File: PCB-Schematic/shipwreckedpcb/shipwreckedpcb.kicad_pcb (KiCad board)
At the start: 4 copper layers, 61.8 x 79.6 mm, 153 parts, among them J1 USB4105, J2 Waveshare 1.54" E-Ink, J3 GPIO, J4 GPIO, J5 SWD, Q1 Si1308EDL, SW1 BOOTSEL, SW10 Resistive, SW11 Clicky - THT, SW12 Clicky - SMD, SW13 Clicky - THT, SW14 Clicky - SMD, SW15 Clicky - THT, SW16 Clicky - SMD, SW17 Clicky - THT, SW18 Clicky - SMD, SW19 PWR Switch, SW2 RESET, SW3 Resistive, SW4 Resistive, SW5 Resistive, SW6 Resistive, SW7 Resistive, SW8 Resistive, SW9 Resistive, U1 RP2040, U2 W25Q128JVS, U3 Si4463, U4 TPS61200DRC, U5 AS179-92LF, U7 PCA9555PW, U8 ST25DV04K-IE6S3, Y1 ABM8-272-T3, Y2 X322530MOB4SI

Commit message: finish placing components
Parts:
- added J14: Conn_01x01, Connector_Wire:SolderWirePad_1x01_SMD_1x2mm, B.Cu at (117.6, 93.7)
- added J15: Conn_01x01, Connector_Wire:SolderWirePad_1x01_SMD_1x2mm, B.Cu at (117.6, 95.5)
- added J16: Conn_01x01, Connector_Wire:SolderWirePad_1x01_SMD_1x2mm, B.Cu at (117.6, 97.3)
- added J17: Conn_01x01, Connector_Wire:SolderWirePad_1x01_SMD_1x2mm, B.Cu at (117.6, 99.1)
- added J18: Conn_01x01, Connector_Wire:SolderWirePad_1x01_SMD_1x2mm, B.Cu at (117.6, 100.9)
- added J19: Conn_01x01, Connector_Wire:SolderWirePad_1x01_SMD_1x2mm, B.Cu at (117.6, 102.7)
- added J20: Conn_01x01, Connector_Wire:SolderWirePad_1x01_SMD_1x2mm, B.Cu at (117.6, 104.5)
- added J21: Conn_01x01, Connector_Wire:SolderWirePad_1x01_SMD_1x2mm, B.Cu at (117.6, 106.3)
- added J22: Conn_01x01, Connector_Wire:SolderWirePad_1x01_SMD_1x2mm, B.Cu at (117.6, 108.1)
- added J23: Conn_01x01, Connector_Wire:SolderWirePad_1x01_SMD_1x2mm, B.Cu at (117.6, 109.9)
- added J24: Conn_01x01, Connector_Wire:SolderWirePad_1x01_SMD_1x2mm, B.Cu at (117.6, 111.7)
- added J25: Conn_01x01, Connector_Wire:SolderWirePad_1x01_SMD_1x2mm, B.Cu at (117.6, 113.6)
- added J26: Conn_01x01, Connector_Wire:SolderWirePad_1x01_SMD_1x2mm, B.Cu at (117.6, 115.4)
- added J28: Conn_01x01, Connector_Wire:SolderWirePad_1x01_SMD_1x2mm, B.Cu at (117.6, 117.2)
- added J29: Conn_01x01, Connector_Wire:SolderWirePad_1x01_SMD_1x2mm, B.Cu at (176.3, 127.8)
- added J30: Conn_01x01, Connector_Wire:SolderWirePad_1x01_SMD_1x2mm, B.Cu at (176.3, 125.4)
- added J31: Conn_01x01, Connector_Wire:SolderWirePad_1x01_SMD_1x2mm, B.Cu at (176.4, 102.0)
- added J32: Conn_01x01, Connector_Wire:SolderWirePad_1x01_SMD_1x2mm, B.Cu at (176.4, 100.2)
- added J33: Conn_01x01, Connector_Wire:SolderWirePad_1x01_SMD_1x2mm, B.Cu at (176.4, 98.4)
- added J34: Conn_01x01, Connector_Wire:SolderWirePad_1x01_SMD_1x2mm, B.Cu at (176.4, 96.5)
- added J35: Conn_01x01, Connector_Wire:SolderWirePad_1x01_SMD_1x2mm, B.Cu at (176.4, 94.7)
- added J36: Conn_01x01, Connector_Wire:SolderWirePad_1x01_SMD_1x2mm, B.Cu at (176.4, 92.8)
- added J37: Conn_01x01, Connector_Wire:SolderWirePad_1x01_SMD_1x2mm, B.Cu at (176.4, 91.0)
- added J38: Conn_01x01, Connector_Wire:SolderWirePad_1x01_SMD_1x2mm, B.Cu at (176.4, 89.1)
- added J39: Conn_01x01, Connector_Wire:SolderWirePad_1x01_SMD_1x2mm, B.Cu at (176.4, 87.3)
- added J6: Conn_01x01, Connector_Wire:SolderWirePad_1x01_SMD_1x2mm, B.Cu at (117.6, 90.1)
- added J7: Conn_01x01, Connector_Wire:SolderWirePad_1x01_SMD_1x2mm, B.Cu at (117.6, 91.9)
- C25, C26, C27, C28, C29, C30, C31, C32, C33, C34, C35, C36, C37, C38, C39, C40, D21, D22, D23, D24, D25, D26, D27, D28, D29, D30, D31, D32, D33, D34, D35, D36, R10, R11, R12, R13, R14, R15, R16, R17: moved to B.Cu
- J3, J4: value GPIO -> Conn_01x01; footprint Connector_PinSocket_2.54mm:PinSocket_1x18_P2.54mm_Vertical -> Connector_Wire:SolderWirePad_1x01_SMD_1x2mm; moved to B.Cu
- moved C26 164.2 mm to (170.0, 120.2)
- moved C32 163.5 mm to (169.9, 86.3)
- moved C27 162.7 mm to (170.2, 109.3)
- moved J4 161.3 mm to (117.6, 88.3), turned to -90 degrees
- moved C28 157.6 mm to (165.6, 100.0), turned to 180 degrees
- moved J3 156.4 mm to (117.6, 86.5), turned to -90 degrees
- moved C31 154.3 mm to (160.4, 82.9), turned to 180 degrees
- moved C34 153.1 mm to (158.6, 130.5), turned to 180 degrees
- moved C30 144.6 mm to (151.0, 82.6), turned to -90 degrees
- moved C36 140.1 mm to (146.2, 131.5)
- moved D25 137.2 mm to (169.9, 89.2), turned to 180 degrees
- moved D21 131.9 mm to (170.0, 134.2), turned to 180 degrees
- moved C25 131.3 mm to (170.1, 131.4), turned to 0 degrees
- moved D24 131.2 mm to (169.2, 100.0), turned to -90 degrees
- moved D23 128.8 mm to (170.2, 112.1), turned to 180 degrees
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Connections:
- J4 pad 1: Earth -> +3V3
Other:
- outline, holes or cut-outs redrawn

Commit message: start routing
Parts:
- moved C29 4.95 mm to (132.3, 85.4), turned to -90 degrees
- moved C2 1.64 mm to (153.9, 108.8)
- moved R6 1.59 mm to (151.7, 111.2), turned to 90 degrees
- moved R1 0.74 mm to (152.9, 105.8)
- moved C7 0.57 mm to (152.4, 107.3)
- moved C15 0.53 mm to (150.8, 123.0)
- moved Q1 0.53 mm to (154.5, 123.0)
- moved R9 0.53 mm to (152.3, 123.0)
- moved C16 0.53 mm to (145.9, 123.0)
- moved C17 0.53 mm to (144.4, 123.0)
- moved C18 0.53 mm to (142.9, 123.0)
- moved C19 0.53 mm to (141.4, 123.0)
- moved C20 0.53 mm to (139.9, 123.0)
- moved C51 0.46 mm to (142.7, 72.5)
- moved C1 0.42 mm to (140.2, 105.5)
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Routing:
- net /SI_NSEL: track 0.00 -> 71.3 mm, vias 0 -> 2
- net /SI_NIRQ: track 0.00 -> 71.2 mm, vias 0 -> 2
- net /I2C_SDA: track 0.00 -> 46.8 mm, vias 0 -> 4
- net /I2C_SCL: track 0.00 -> 46.0 mm, vias 0 -> 4
- net /USB_DM: track 0.00 -> 42.3 mm, vias 0 -> 2
- net /USB_DP: track 0.00 -> 41.7 mm, vias 0 -> 2
- net /SPI_MISO: track 0.00 -> 31.4 mm
- net /SPI_MOSI: track 0.00 -> 28.3 mm, vias 0 -> 2
- net /SPI_CLK: track 0.00 -> 26.7 mm
- net /IO_INT: track 0.00 -> 26.6 mm
- net Net-(D4-A): track 0.00 -> 25.6 mm
- net /DISP_PREVGL: track 0.00 -> 20.3 mm, vias 0 -> 2
- net +3V3: track 0.00 -> 19.4 mm
- net /QSPI_SD3: track 0.00 -> 17.9 mm, vias 0 -> 2
- net /QSPI_SCLK: track 0.00 -> 15.6 mm, vias 0 -> 2
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
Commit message: production files (tentative)
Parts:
- moved SW19 16.9 mm to (133.9, 64.2), turned to 0 degrees
- moved C55 11.5 mm to (119.0, 68.3), turned to 90 degrees
- moved R18 11.4 mm to (121.5, 72.0), turned to 0 degrees
- moved R19 10.6 mm to (123.8, 72.7), turned to -90 degrees
- moved C54 9.53 mm to (120.5, 68.3), turned to 90 degrees
- moved C52 7.59 mm to (122.0, 68.3), turned to -90 degrees
- moved U4 5.15 mm to (124.9, 69.0), turned to -90 degrees
- moved C53 3.76 mm to (127.8, 68.3), turned to 90 degrees
- moved L9 1.68 mm to (126.1, 64.9), turned to 180 degrees
- moved L8 0.73 mm to (168.4, 68.3)
- moved C50 0.73 mm to (166.9, 66.9)
- moved C44 0.73 mm to (165.0, 69.0)
- moved C49 0.73 mm to (166.9, 69.0)
- moved L7 0.73 mm to (166.9, 67.8)
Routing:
- net /SI_IO1: track 0.00 -> 69.5 mm, vias 0 -> 2
- net /SI_SDN: track 0.00 -> 60.5 mm
- net /SI_V1: track 0.00 -> 22.9 mm, vias 0 -> 2
- net /SI_V2: track 0.00 -> 19.3 mm, vias 0 -> 2
- net Net-(U5-J2): track 0.00 -> 8.99 mm
- net /SI_RXn: track 0.00 -> 4.37 mm
- net /SI_RXp: track 0.00 -> 3.67 mm
- net /SI_TX: track 0.00 -> 3.55 mm
- net Net-(AE1-A): track 0.00 -> 3.54 mm
- net Net-(C44-Pad1): track 0.00 -> 2.04 mm
- net Net-(C42-Pad2): track 0.00 -> 1.98 mm
- net Net-(C43-Pad2): track 0.00 -> 1.97 mm
- net Net-(C46-Pad2): track 0.00 -> 1.94 mm
- net Earth: track 4.95 -> 6.88 mm
- net Net-(U5-J3): track 0.00 -> 1.13 mm
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
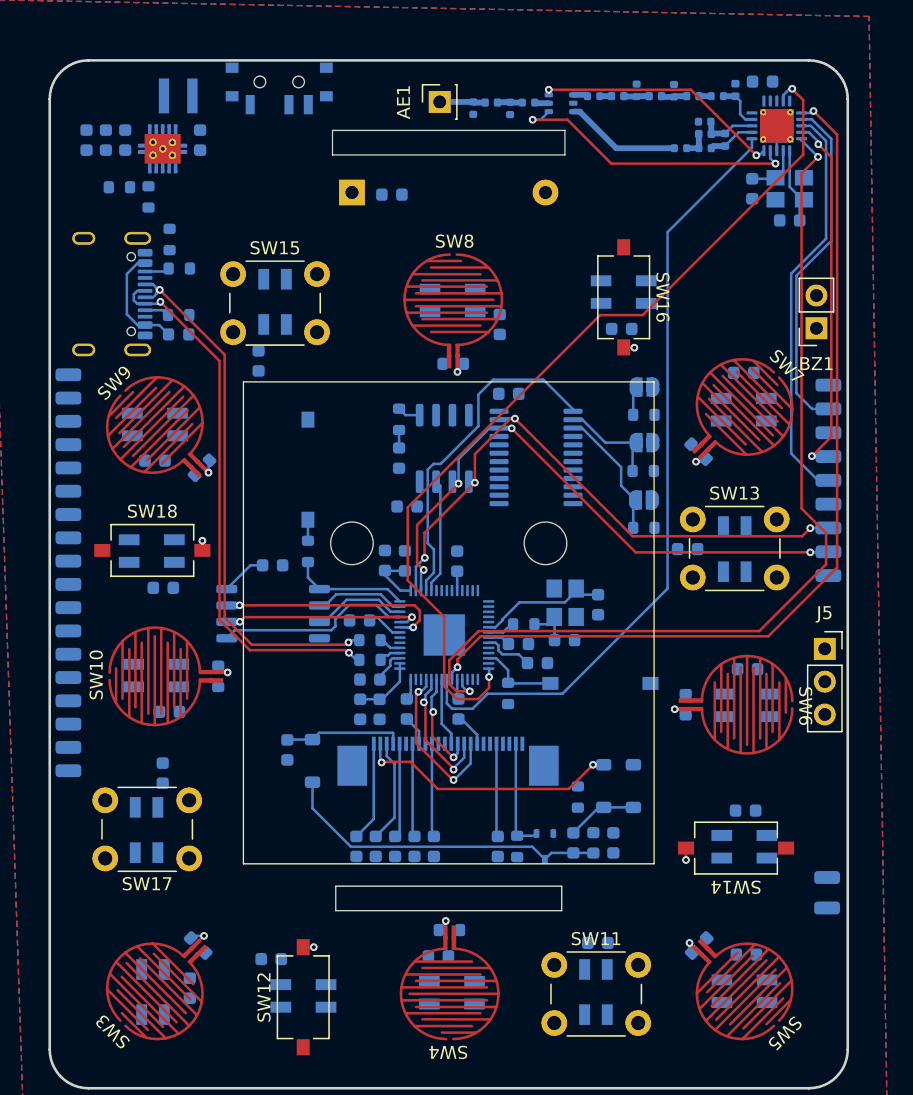
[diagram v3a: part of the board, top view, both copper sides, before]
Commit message: boost conv, leds, caps, added ldo for usb
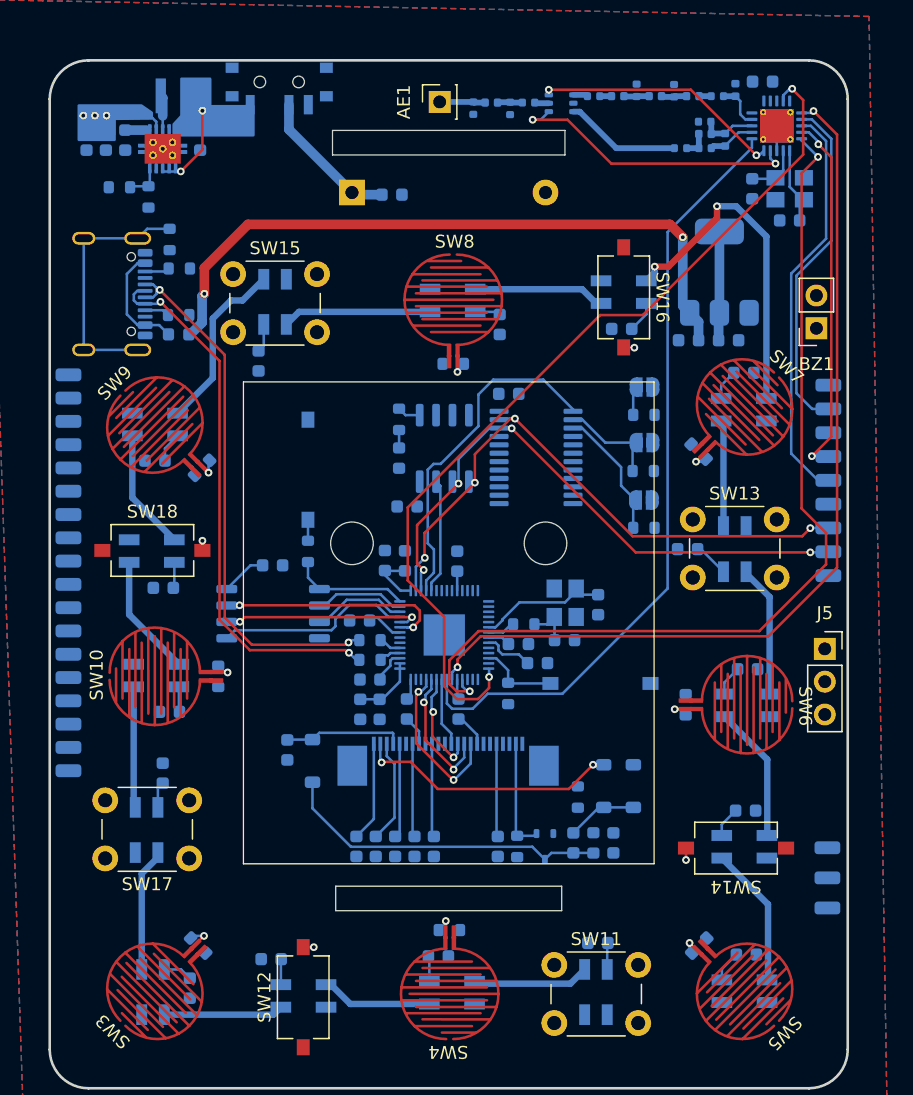
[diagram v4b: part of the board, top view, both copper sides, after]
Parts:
- added C60: 10uF, Capacitor_SMD:C_0603_1608Metric, B.Cu at (168.7, 83.8)
- added C61: 10uF, Capacitor_SMD:C_0603_1608Metric, B.Cu at (165.6, 83.8)
- added J40: Conn_01x01, Connector_Wire:SolderWirePad_1x01_SMD_1x2mm, B.Cu at (176.4, 123.1)
- added U6: AMS1117-3.3, Package_TO_SOT_SMD:SOT-223-3_TabPin2, B.Cu at (168.0, 78.5)
- moved L9 0.25 mm to (125.8, 64.9)
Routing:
- net +5V: track 0.00 -> 53.1 mm, vias 0 -> 2
- net +3V3: track 19.4 -> 65.6 mm, vias 0 -> 3
- net Net-(D25-DOUT): track 0.00 -> 26.0 mm, vias 0 -> 2
- net Net-(J1-SHIELD): track 0.00 -> 19.8 mm
- net Net-(D28-DOUT): track 0.00 -> 13.7 mm
- net Net-(D27-DOUT): track 0.00 -> 11.5 mm
- net /BT Power: track 0.00 -> 11.2 mm
- net Net-(D21-DOUT): track 0.00 -> 11.0 mm
- net Net-(D22-DOUT): track 0.00 -> 10.6 mm
- net Net-(D23-DOUT): track 0.00 -> 10.2 mm
- net Net-(D26-DOUT): track 0.00 -> 10.2 mm
- net Net-(D35-DOUT): track 0.00 -> 9.57 mm
- net Net-(D31-DOUT): track 0.00 -> 9.48 mm
- net Net-(D29-DOUT): track 0.00 -> 9.40 mm
- net Net-(D33-DOUT): track 0.00 -> 9.39 mm
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
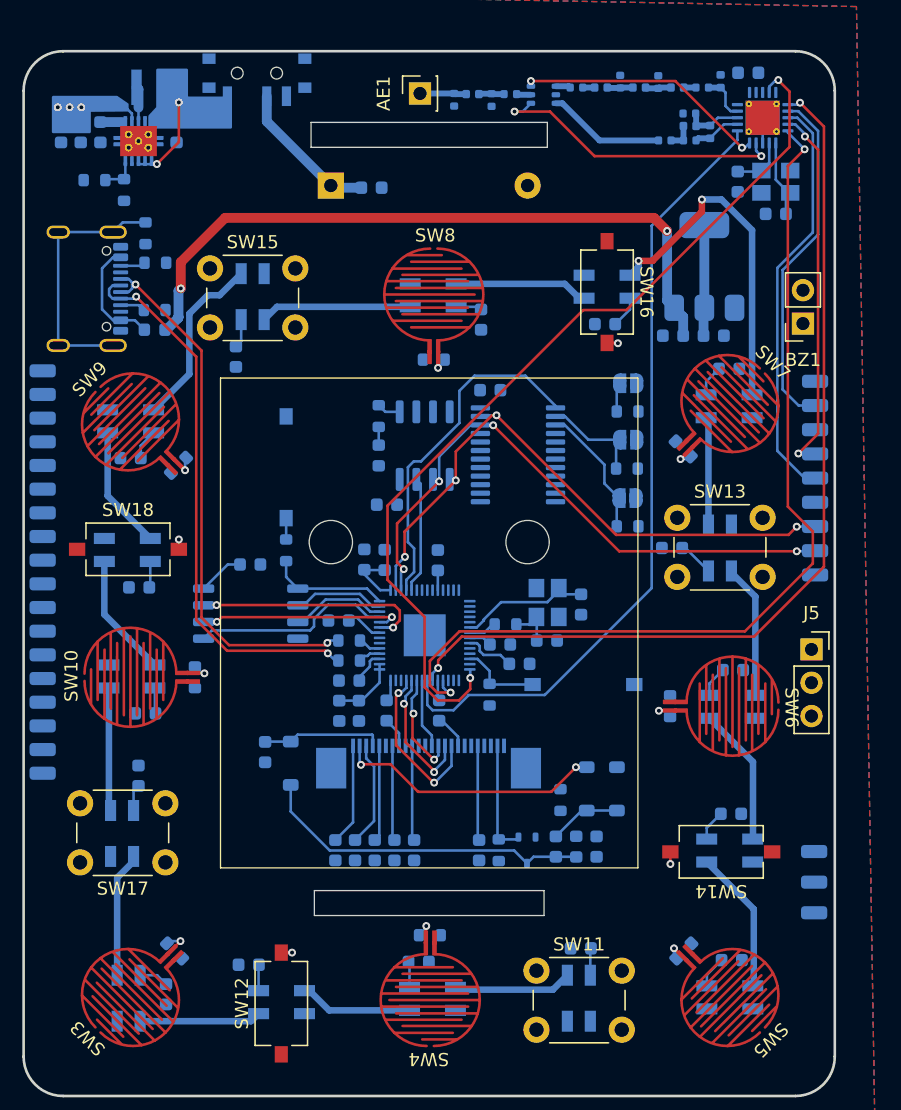
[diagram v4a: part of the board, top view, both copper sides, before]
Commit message: finished buttons, removed nfc, routed interface headers
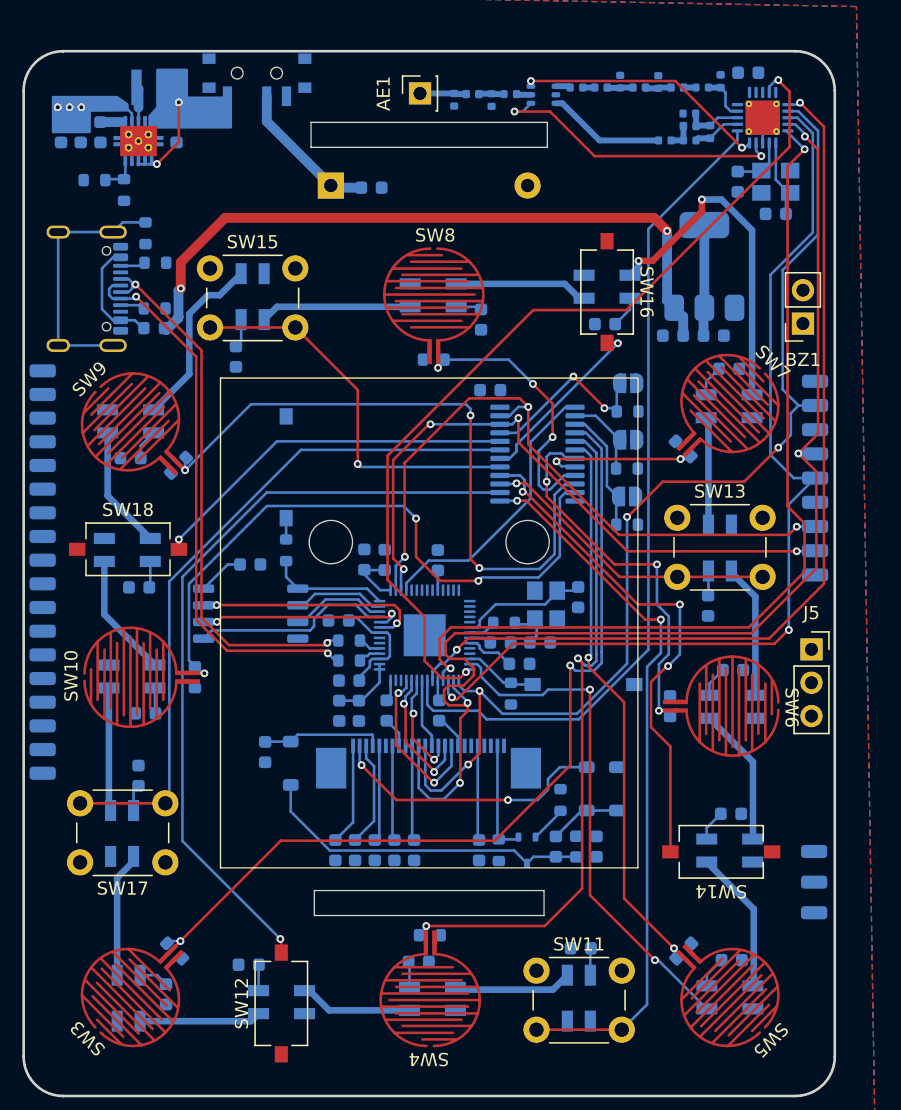
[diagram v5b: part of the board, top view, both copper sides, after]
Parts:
- removed C57: 100nF, Capacitor_SMD:C_0603_1608Metric
- removed D5: LED, LED_SMD:LED_0603_1608Metric
- removed R23: 47, Resistor_SMD:R_0603_1608Metric
- removed U8: ST25DV04K-IE6S3, Package_SO:SO-8_3.9x4.9mm_P1.27mm
- moved C28 5.19 mm to (168.3, 104.4), turned to -90 degrees
- moved R6 1.63 mm to (153.3, 111.1)
- moved U7 1.49 mm to (155.3, 92.8)
- moved C13 0.59 mm to (158.4, 103.8)
- moved C14 0.54 mm to (155.5, 107.2)
- moved Y1 0.23 mm to (155.9, 104.3)
- moved R1 0.16 mm to (152.8, 105.7)
- moved C7 0.15 mm to (152.5, 107.2)
- moved JP3 0.13 mm to (162.1, 96.1)
- moved R22 0.13 mm to (162.1, 98.2)
- moved D1 0.13 mm to (126.1, 83.2)
- moved R4 0.12 mm to (126.1, 81.8)
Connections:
- U1 pad 5: /NFC_GPO -> /GPIO3
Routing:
- net /SPI_MOSI: track 28.3 -> 93.5 mm, vias 2 -> 4
- net /BUTT_1: track 2.48 -> 67.0 mm, vias 1 -> 2
- net /BUTT_10: track 0.82 -> 58.6 mm
- net /SPI_CLK: track 26.7 -> 84.4 mm, vias 0 -> 4
- net /BUTT_9: track 0.00 -> 55.0 mm, vias 0 -> 2
- net /BUTT_15: track 0.00 -> 52.9 mm
- net /BUTT_2: track 2.23 -> 52.6 mm, vias 1 -> 2
- net /BUTT_7: track 2.19 -> 51.2 mm, vias 1 -> 3
- net /BUTT_8: track 2.24 -> 50.0 mm, vias 1 -> 3
- net /SPI_MISO: track 31.4 -> 74.1 mm, vias 0 -> 2
- net /BUTT_3: track 2.17 -> 43.9 mm, vias 1 -> 2
- net /RGB_DIN: track 0.00 -> 38.8 mm, vias 0 -> 2
- net /BUTT_12: track 0.92 -> 39.0 mm, vias 1 -> 3
- net /BUTT_13: track 0.00 -> 29.8 mm, vias 0 -> 1
- net /BUTT_4: track 2.31 -> 30.1 mm, vias 1 -> 3
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
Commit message: made some progress with the expansion headers
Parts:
- moved C7 0.89 mm to (153.3, 107.0)
- moved C14 0.87 mm to (156.3, 107.0)
- moved C2 0.50 mm to (154.3, 108.5)
- moved R6 0.44 mm to (153.6, 111.4)
- moved SW2 0.43 mm to (159.2, 110.7)
- moved R1 0.36 mm to (152.4, 105.5)
- moved Y1 0.20 mm to (155.9, 104.2)
- moved C9 0.16 mm to (143.7, 112.4)
- moved C1 0.13 mm to (140.1, 105.7)
- moved R2 0.10 mm to (140.9, 107.2)
- moved R3 0.08 mm to (140.9, 108.7)
- moved C3 0.05 mm to (140.9, 110.2)
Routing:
- net /GPIO13: track 0.00 -> 46.1 mm, vias 0 -> 2
- net /GPIO14: track 0.00 -> 39.4 mm, vias 0 -> 2
- net /GPIO15: track 0.00 -> 38.3 mm, vias 0 -> 2
- net /GPIO29_ADC3: track 0.00 -> 30.8 mm, vias 0 -> 2
- net /RP_SWDIO: track 0.00 -> 30.0 mm, vias 0 -> 1
- net /RP_SWCLK: track 0.00 -> 27.8 mm, vias 0 -> 1
- net /SI_IO1: track 68.2 -> 65.1 mm
- net /QSPI_SCLK: track 16.0 -> 13.4 mm
- net /IO_INT: track 21.5 -> 23.2 mm
- net /I2C_SDA: track 52.0 -> 53.7 mm
- net /QSPI_SD3: track 17.6 -> 19.3 mm
- net /SPI_MOSI: track 93.5 -> 92.4 mm
- net /BUTT_8: track 50.0 -> 49.3 mm
- net +3V3: track 64.8 -> 65.4 mm
- net /BUTT_7: track 51.2 -> 50.5 mm
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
